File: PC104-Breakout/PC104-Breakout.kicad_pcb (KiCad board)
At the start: 2 copper layers, 150 x 100 mm, 9 parts, among them J1 Screw_Terminal_01x02, J2 Screw_Terminal_01x02, J3 Screw_Terminal_01x02

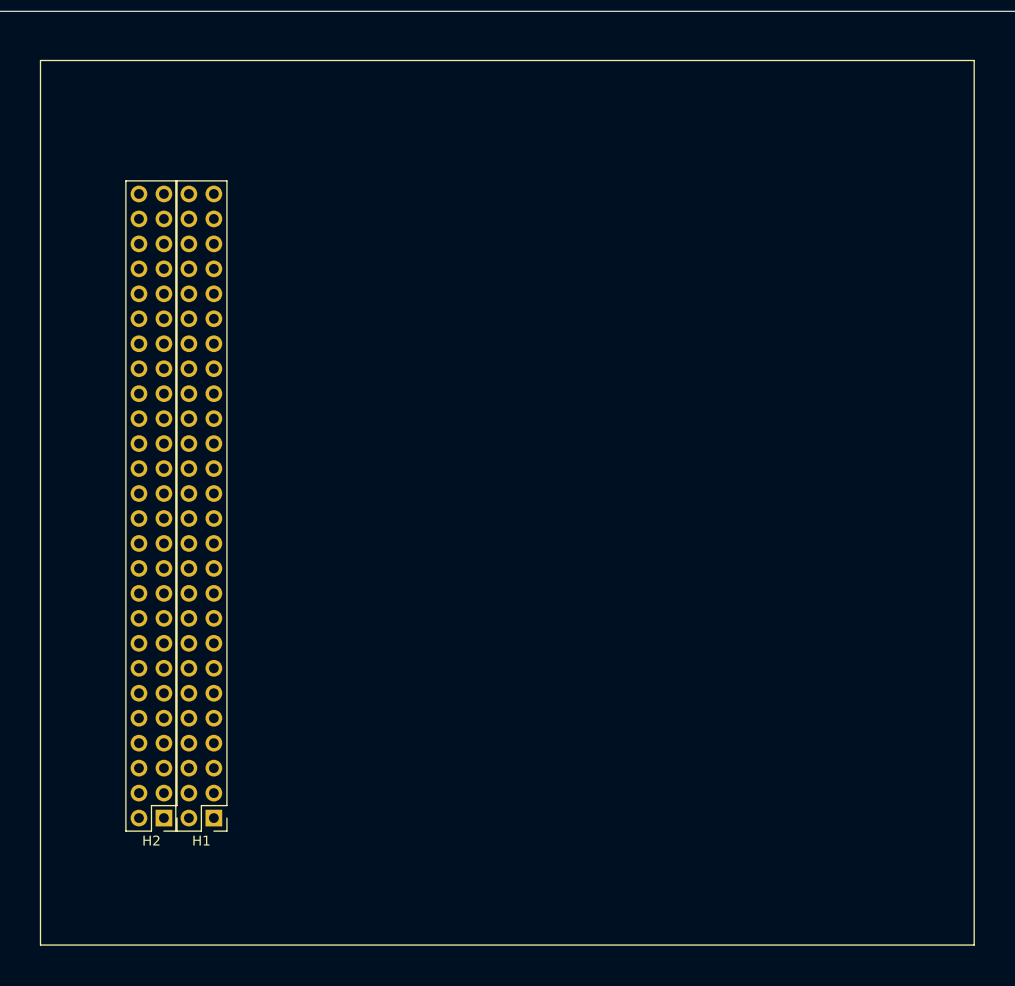
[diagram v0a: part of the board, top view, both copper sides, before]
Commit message: added screwholes
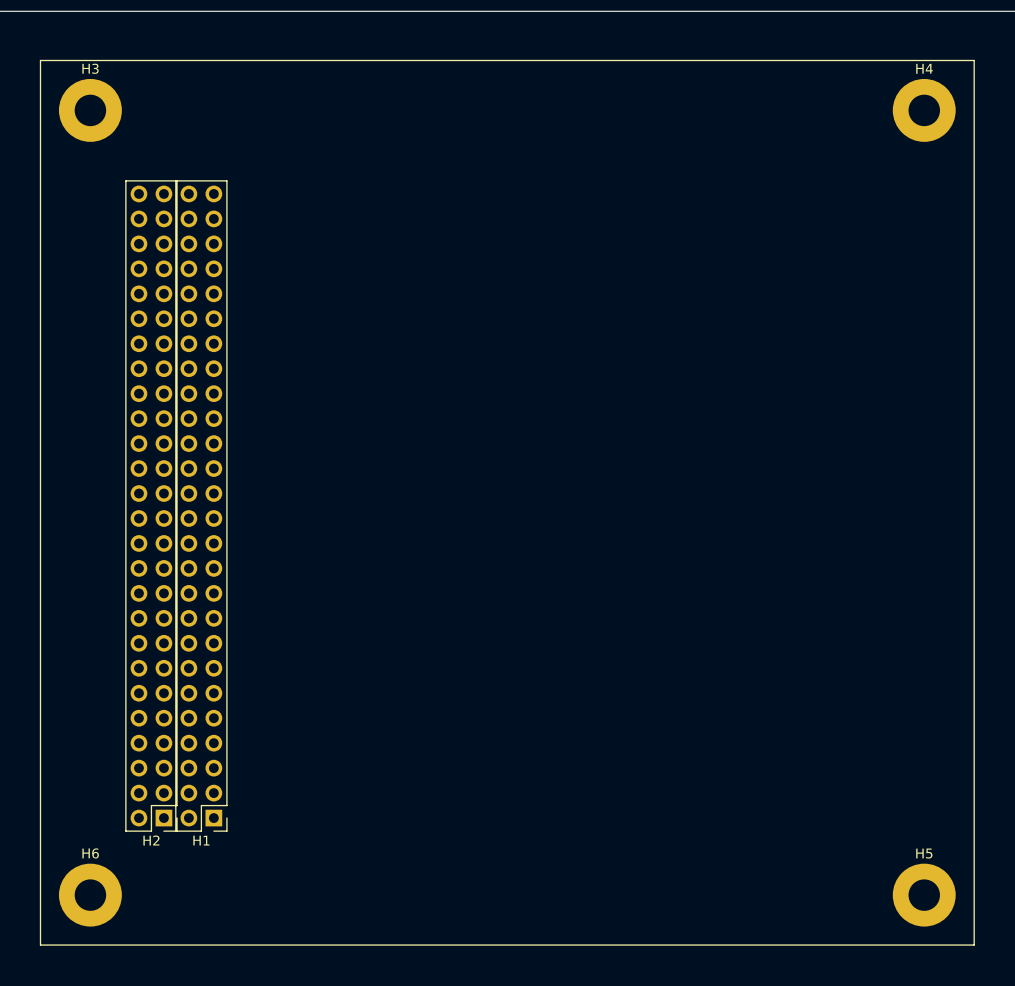
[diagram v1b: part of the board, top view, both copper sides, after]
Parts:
- added H3: MountingHole_Pad, MountingHole:MountingHole_3.2mm_M3_Pad, F.Cu at (155.1, 60.1)
- added H4: MountingHole_Pad, MountingHole:MountingHole_3.2mm_M3_Pad, F.Cu at (239.9, 60.1)
- added H5: MountingHole_Pad, MountingHole:MountingHole_3.2mm_M3_Pad, F.Cu at (239.9, 139.9)
- added H6: MountingHole_Pad, MountingHole:MountingHole_3.2mm_M3_Pad, F.Cu at (155.1, 139.9)

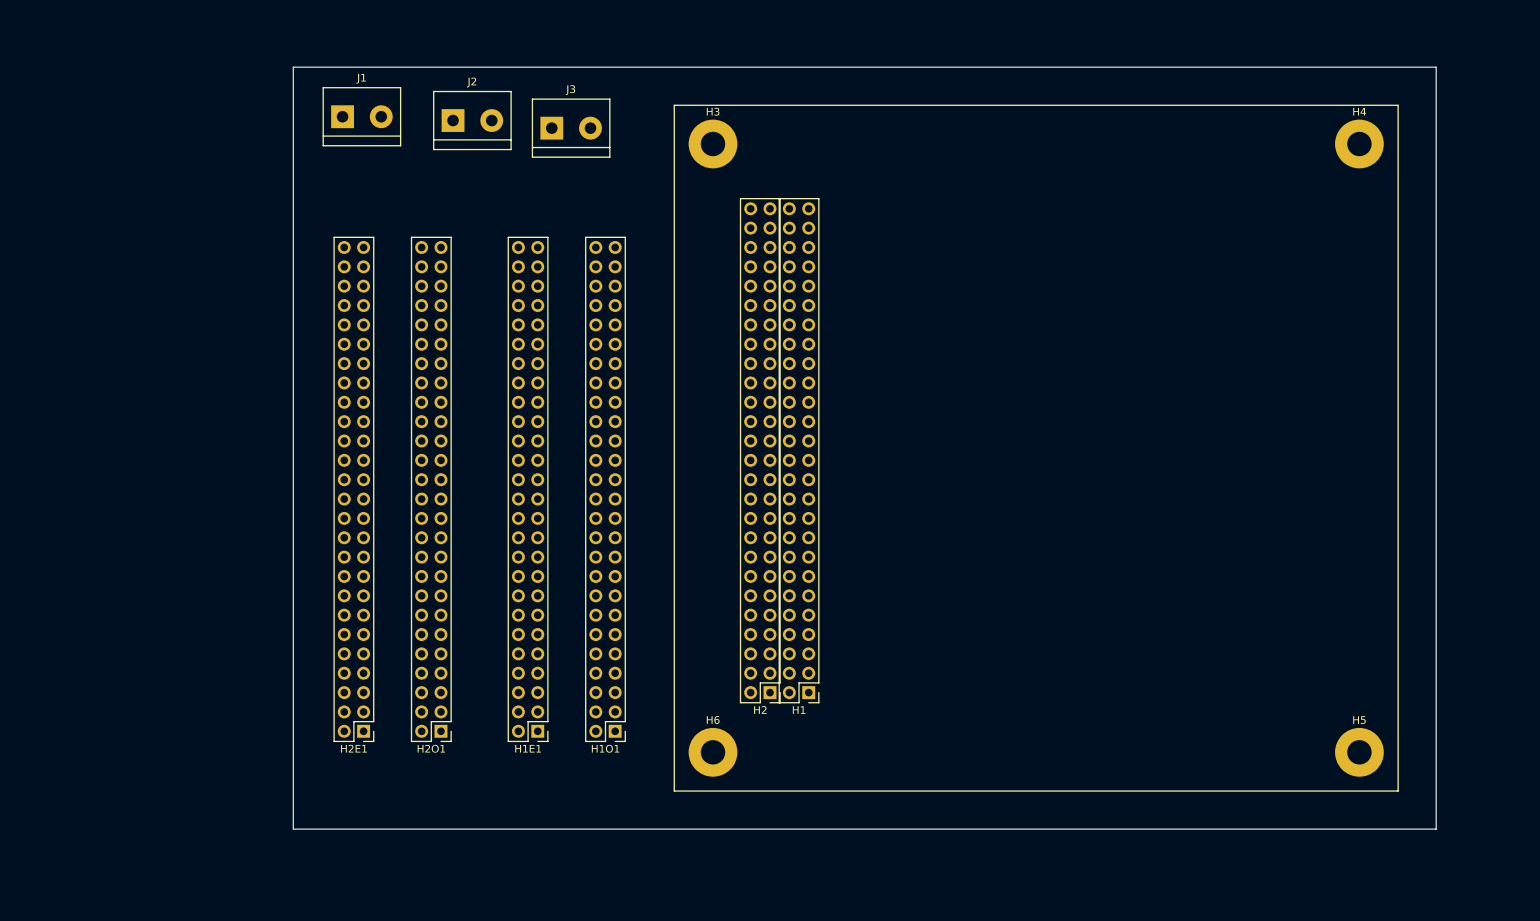
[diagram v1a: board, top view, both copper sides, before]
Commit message: added silk screens for header pins
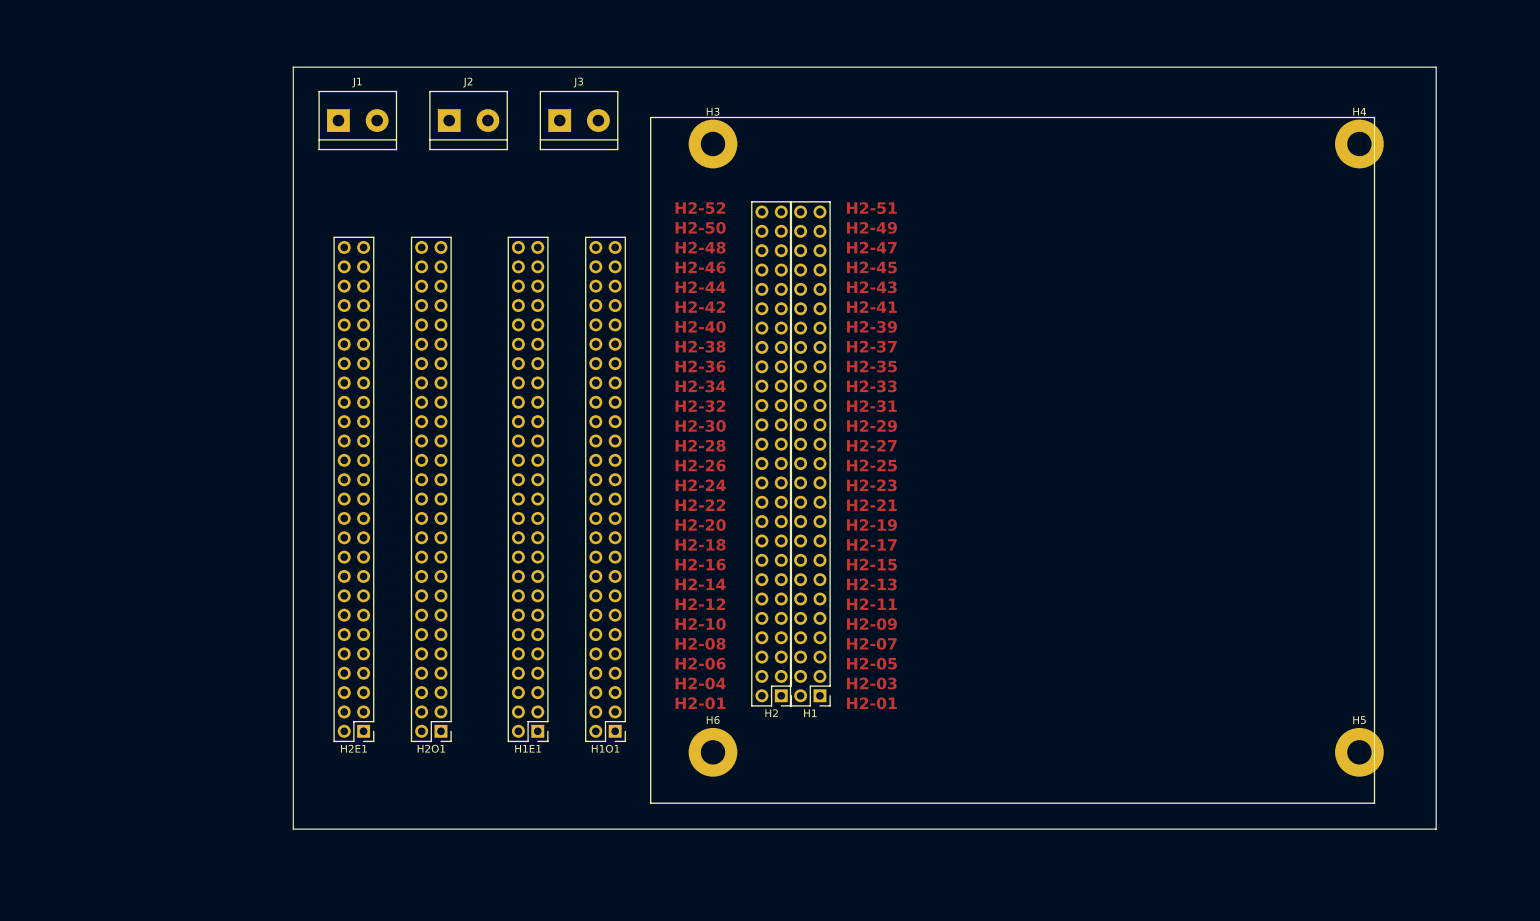
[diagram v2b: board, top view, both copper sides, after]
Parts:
- moved H1 1.54 mm to (169.1, 132.5)
- moved H2 1.54 mm to (164.0, 132.5)
- moved J3 1.44 mm to (135.0, 57.0)
- moved J1 0.74 mm to (105.9, 57.0)
- moved J2 0.50 mm to (120.5, 57.0)
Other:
- board text added: "H2-01"
- board text added: "H2-03"
- board text added: "H2-04"
- board text added: "H2-05"
- board text added: "H2-06"
- board text added: "H2-07"
- board text added: "H2-08"
- board text added: "H2-09"
- board text added: "H2-10"
- board text added: "H2-11"
- board text added: "H2-12"
- board text added: "H2-13"
- board text added: "H2-14"
- board text added: "H2-15"
- board text added: "H2-16"
- board text added: "H2-17"
- board text added: "H2-18"
- board text added: "H2-19"
- board text added: "H2-20"
- board text added: "H2-21"
- board text added: "H2-22"
- board text added: "H2-23"
- board text added: "H2-24"
- board text added: "H2-25"
- board text added: "H2-26"
- board text added: "H2-27"
- board text added: "H2-28"
- board text added: "H2-29"
- board text added: "H2-30"
- board text added: "H2-31"
- board text added: "H2-32"
- board text added: "H2-33"
- board text added: "H2-34"
- board text added: "H2-35"
- board text added: "H2-36"
- board text added: "H2-37"
- board text added: "H2-38"
- board text added: "H2-39"
- board text added: "H2-40"
- board text added: "H2-41"
- board text added: "H2-42"
- board text added: "H2-43"
- board text added: "H2-44"
- board text added: "H2-45"
- board text added: "H2-46"
- board text added: "H2-47"
- board text added: "H2-48"
- board text added: "H2-49"
- board text added: "H2-50"
- board text added: "H2-51"
- board text added: "H2-52"

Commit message: Positioned external mounting holes
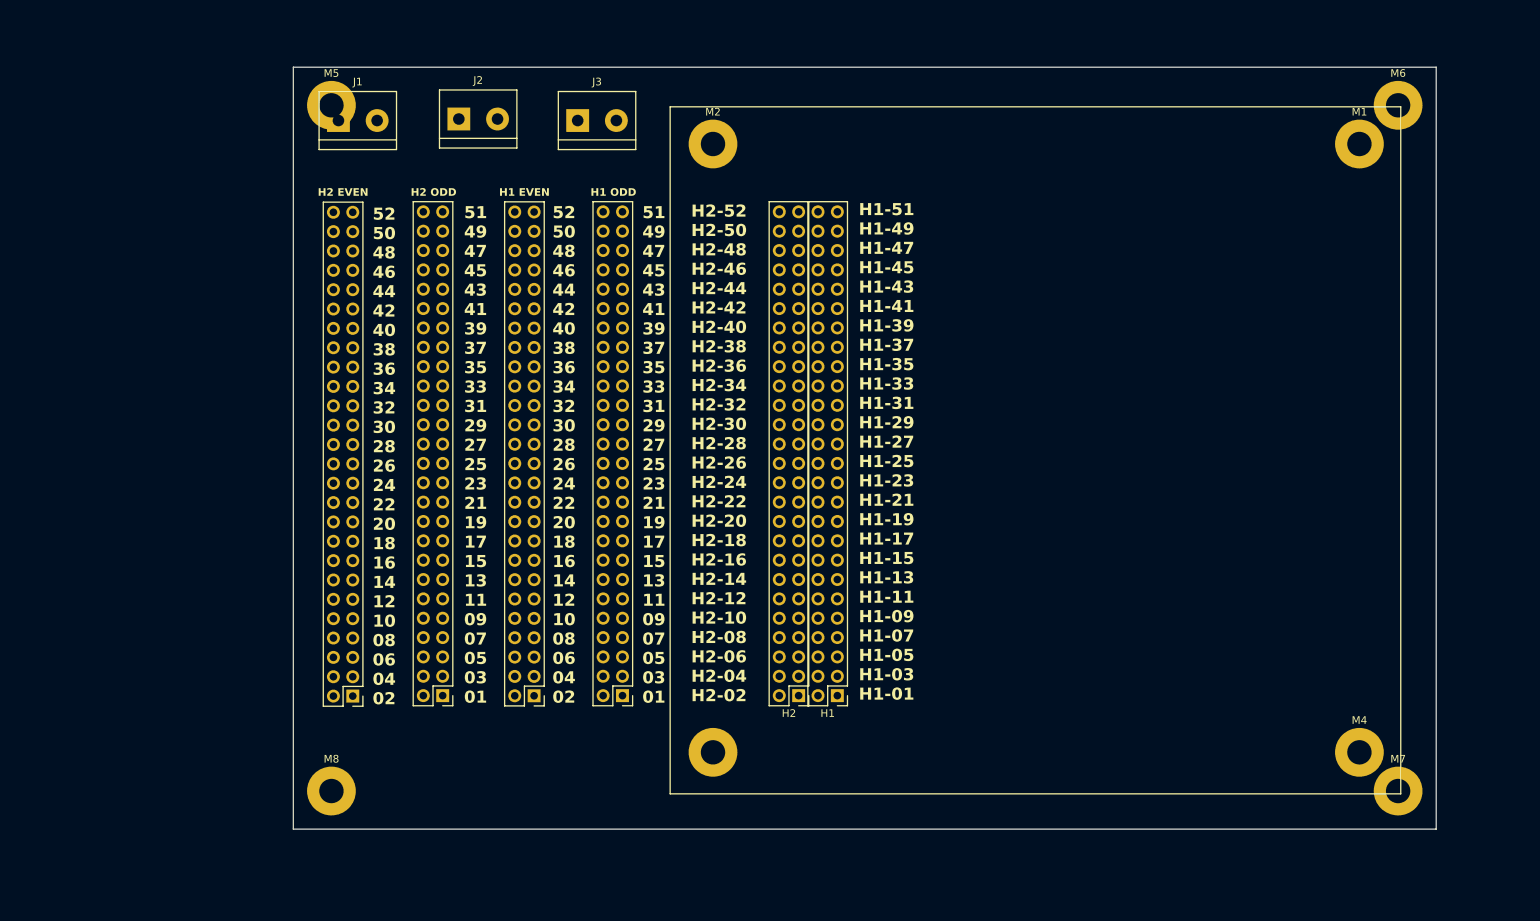
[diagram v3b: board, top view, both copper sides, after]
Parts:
- added M5: MountingHole_Pad, MountingHole:MountingHole_3.2mm_M3_Pad, F.Cu at (105.0, 55.0)
- added M6: MountingHole_Pad, MountingHole:MountingHole_3.2mm_M3_Pad, F.Cu at (245.0, 55.0)
- added M7: MountingHole_Pad, MountingHole:MountingHole_3.2mm_M3_Pad, F.Cu at (245.0, 145.0)
- added M8: MountingHole_Pad, MountingHole:MountingHole_3.2mm_M3_Pad, F.Cu at (105.0, 145.0)
- moved H2E1 4.83 mm to (107.8, 132.5)
- moved H1O1 4.78 mm to (143.2, 132.5)
- moved H2O1 4.69 mm to (119.6, 132.5)
- moved H1E1 4.68 mm to (131.6, 132.5)
- moved J3 2.36 mm to (137.3, 57.0)
- moved H1 2.28 mm to (171.4, 132.5)
- moved H2 2.28 mm to (166.3, 132.5)
- moved J2 1.28 mm to (121.7, 56.8)
- renumbered H4 to M1, H3 to M2, H6 to M3, H5 to M4
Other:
- copper layers 2 -> 4
- board text added: "51 49 47 45 43 41 39 37 35 33 31 29 27 25 23 21 19 17 15 13 11 09 07 05 03 01"
- board text added: "52 50 48 46 44 42 40 38 36 34 32 30 28 26 24 22 20 18 16 14 12 10 08 06 04 02"
- board text added: "H1 EVEN"
- board text added: "H1 ODD"
- board text added: "H1-51 H1-49 H1-47 H1-45 H1-43 H1-41 H1-39 H1-37 H1-35 H1-33 H1-31 H1-29 H1-27 H1-25 H1-23 H1-21 H1-19 H1-17 H1-15 H1-13 H1-11 H1-09 H1-07 H1-05 H1-03 H1-01"
- board text added: "H2 EVEN"
- board text added: "H2 ODD"
- board text added: "H2-52 H2-50 H2-48 H2-46 H2-44 H2-42 H2-40 H2-38 H2-36 H2-34 H2-32 H2-30 H2-28 H2-26 H2-24 H2-22 H2-20 H2-18 H2-16 H2-14 H2-12 H2-10 H2-08 H2-06 H2-04 H2-02"
- board text removed: "H2-01"
- board text removed: "H2-03"
- board text removed: "H2-04"
- board text removed: "H2-05"
- board text removed: "H2-06"
- board text removed: "H2-07"
- board text removed: "H2-08"
- board text removed: "H2-09"
- board text removed: "H2-10"
- board text removed: "H2-11"
- board text removed: "H2-12"
- board text removed: "H2-13"
- board text removed: "H2-14"
- board text removed: "H2-15"
- board text removed: "H2-16"
- board text removed: "H2-17"
- board text removed: "H2-18"
- board text removed: "H2-19"
- board text removed: "H2-20"
- board text removed: "H2-21"
- board text removed: "H2-22"
- board text removed: "H2-23"
- board text removed: "H2-24"
- board text removed: "H2-25"
- board text removed: "H2-26"
- board text removed: "H2-27"
- board text removed: "H2-28"
- board text removed: "H2-29"
- board text removed: "H2-30"
- board text removed: "H2-31"
- board text removed: "H2-32"
- board text removed: "H2-33"
- board text removed: "H2-34"
- board text removed: "H2-35"
- board text removed: "H2-36"
- board text removed: "H2-37"
- board text removed: "H2-38"
- board text removed: "H2-39"
- board text removed: "H2-40"
- board text removed: "H2-41"
- board text removed: "H2-42"
- board text removed: "H2-43"
- board text removed: "H2-44"
- board text removed: "H2-45"
- board text removed: "H2-46"
- board text removed: "H2-47"
- board text removed: "H2-48"
- board text removed: "H2-49"
- board text removed: "H2-50"
- board text removed: "H2-51"
- board text removed: "H2-52"
